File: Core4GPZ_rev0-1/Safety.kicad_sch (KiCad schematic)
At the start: 5 parts

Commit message: Reworked the VR conditionner
Schematic and PCB based on the Dropbear model
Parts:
- renumbered D3 to D1, D4 to D2, D5 to D3, D6 to D4, R6 to R1
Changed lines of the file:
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@@
 		(dnp no)
 		(fields_autoplaced yes)
-		(property "Reference" "R6"
+		(property "Reference" "R1"
 			(at 58.42 36.83 0)
 			(effects
@@
 			(project "Core4GPZ_rev0-1"
 				(path "/ac28f42d-34b3-4fcc-84dd-ab6106f99610/47dee9fe-f537-47a7-b917-fe922e75e357"
-					(reference "R6")
+					(reference "R1")
 					(unit 1)
 				)
@@
 		(on_board yes)
 		(dnp no)
-		(property "Reference" "D3"
+		(property "Reference" "D1"
 			(at 51.308 40.64 0)
 			(effects
@@
 			(project "Core4GPZ_rev0-1"
 				(path "/ac28f42d-34b3-4fcc-84dd-ab6106f99610/47dee9fe-f537-47a7-b917-fe922e75e357"
-					(reference "D3")
+					(reference "D1")
 					(unit 1)
 				)
@@
 		(on_board yes)
 		(dnp no)
-		(property "Reference" "D4"
+		(property "Reference" "D2"
 			(at 51.308 50.8 0)
 			(effects
@@
 			(project "Core4GPZ_rev0-1"
 				(path "/ac28f42d-34b3-4fcc-84dd-ab6106f99610/47dee9fe-f537-47a7-b917-fe922e75e357"
-					(reference "D4")
+					(reference "D2")
 					(unit 1)
 				)
@@
 		(on_board yes)
 		(dnp no)
-		(property "Reference" "D6"
+		(property "Reference" "D4"
 			(at 51.308 71.12 0)
 			(effects
@@
 			(project "Core4GPZ_rev0-1"
 				(path "/ac28f42d-34b3-4fcc-84dd-ab6106f99610/47dee9fe-f537-47a7-b917-fe922e75e357"
-					(reference "D6")
+					(reference "D4")
 					(unit 1)
 				)
@@
 		(dnp no)
 		(fields_autoplaced yes)
-		(property "Reference" "#PWR013"
+		(property "Reference" "#PWR07"
 			(at 55.88 35.56 0)
 			(effects
@@
 			(project "Core4GPZ_rev0-1"
 				(path "/ac28f42d-34b3-4fcc-84dd-ab6106f99610/47dee9fe-f537-47a7-b917-fe922e75e357"
-					(reference "#PWR013")
+					(reference "#PWR07")
 					(unit 1)
 				)
@@
 		(on_board yes)
 		(dnp no)
-		(property "Reference" "D5"
+		(property "Reference" "D3"
 			(at 51.308 60.706 0)
 			(effects
@@
 			(project "Core4GPZ_rev0-1"
 				(path "/ac28f42d-34b3-4fcc-84dd-ab6106f99610/47dee9fe-f537-47a7-b917-fe922e75e357"
-					(reference "D5")
-					(unit 1)
-				)
+					(reference "D3")
+					(unit 1)
+				)

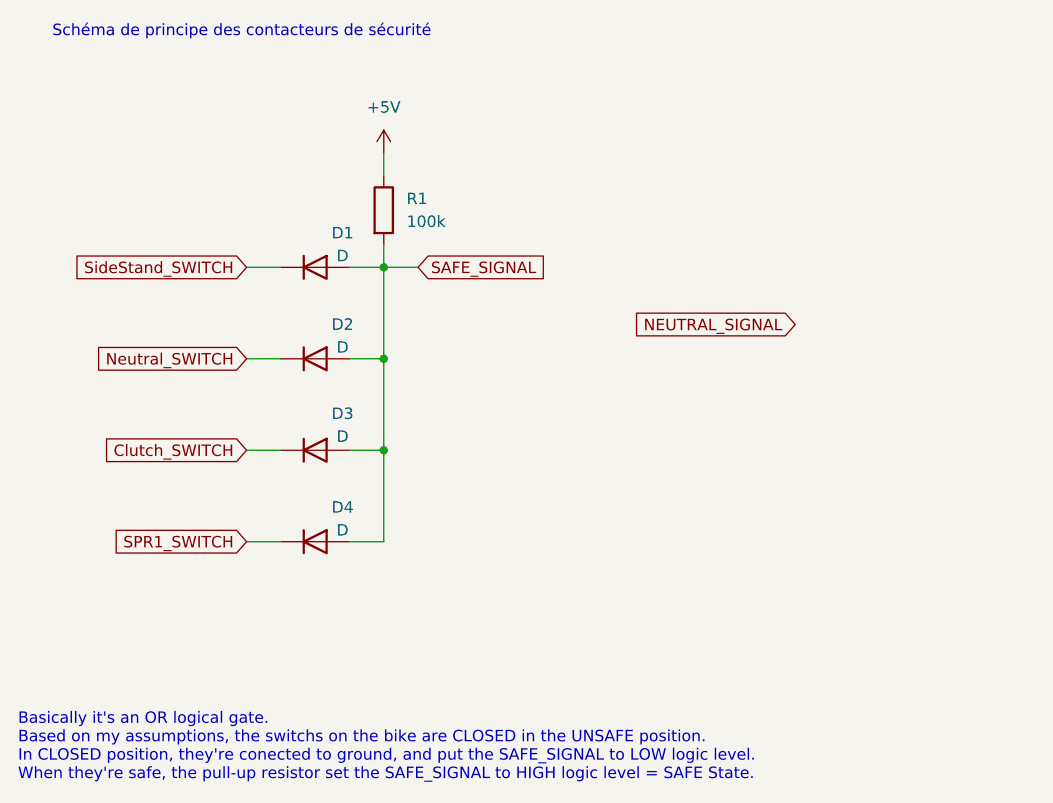
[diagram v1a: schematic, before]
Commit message: Modified GND Plane. Reworked routing
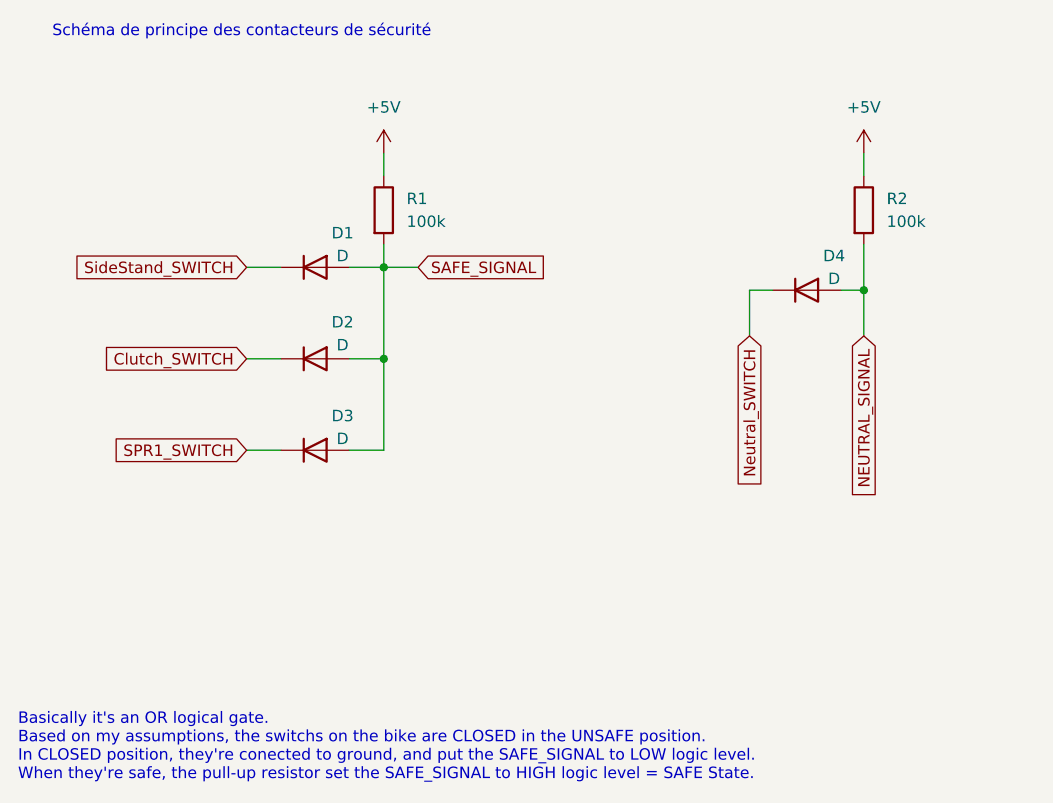
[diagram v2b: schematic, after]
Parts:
- added R2: 100k, Resistor_SMD:R_0603_1608Metric, symbol Device:R
- renumbered D3 to D2, D4 to D3, D2 to D4
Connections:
- net +5V: now also R2.1
- net NEUTRAL_SIGNAL: now also D4.2 (A), R2.2
- net SAFE_SIGNAL: no longer D4.2 (A)
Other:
- moved on the sheet: D2, D3, D4

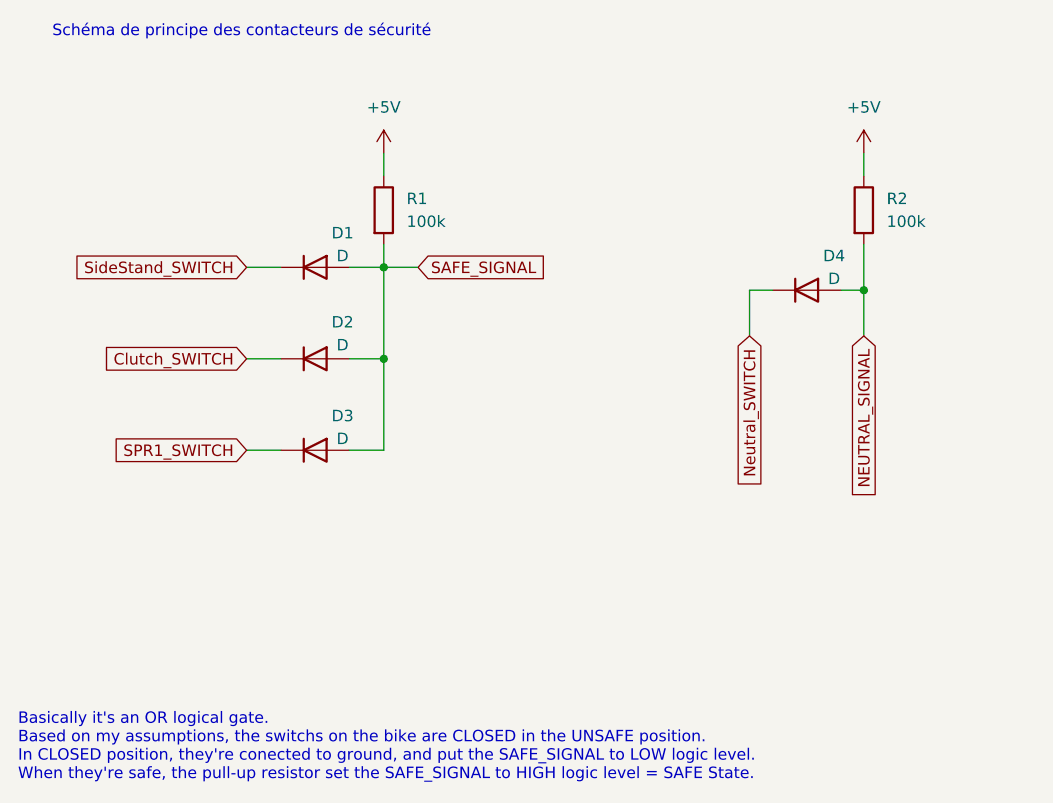
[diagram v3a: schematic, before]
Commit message: Removed NeutralSwitch. Added Up-Shifter support
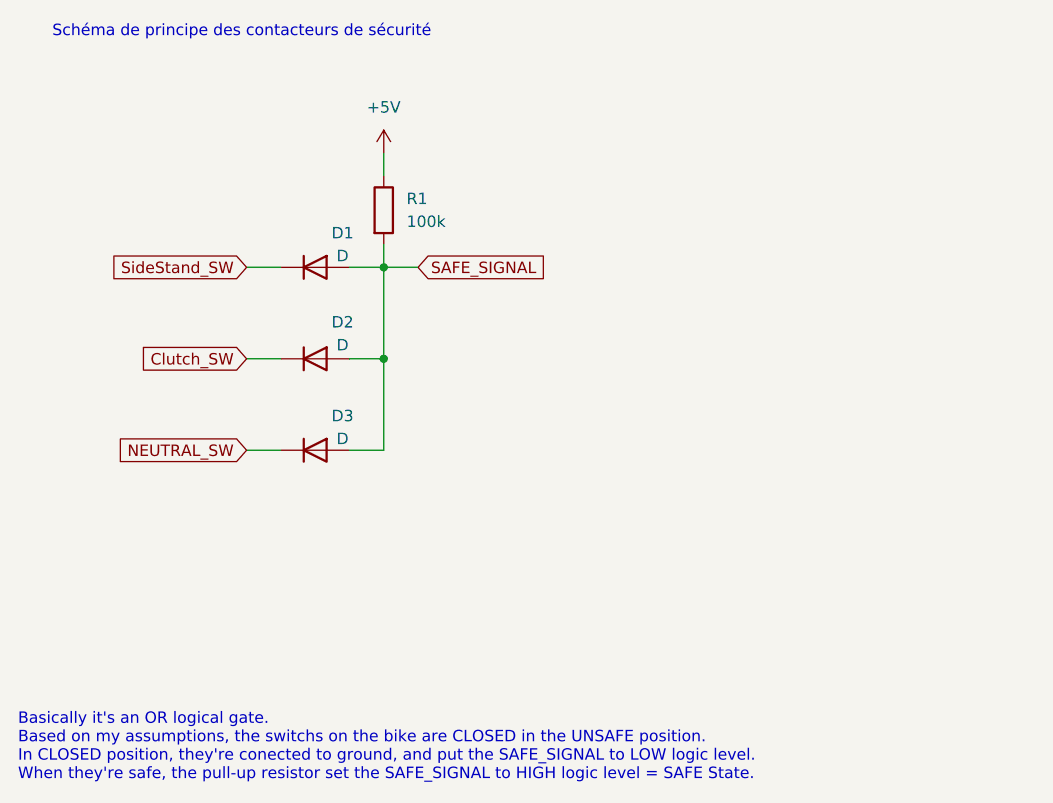
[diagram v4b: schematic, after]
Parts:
- removed D4: D, Diode_SMD:D_0603_1608Metric, symbol Device:D
- removed R2: 100k, Resistor_SMD:R_0603_1608Metric, symbol Device:R
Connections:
- net Clutch_SWITCH renamed Clutch_SW
- net SPR1_SWITCH renamed NEUTRAL_SW
- net SideStand_SWITCH renamed SideStand_SW
